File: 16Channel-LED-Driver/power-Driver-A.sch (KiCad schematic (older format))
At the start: 17 parts, among them Q1 BC413, U3 PCA9634

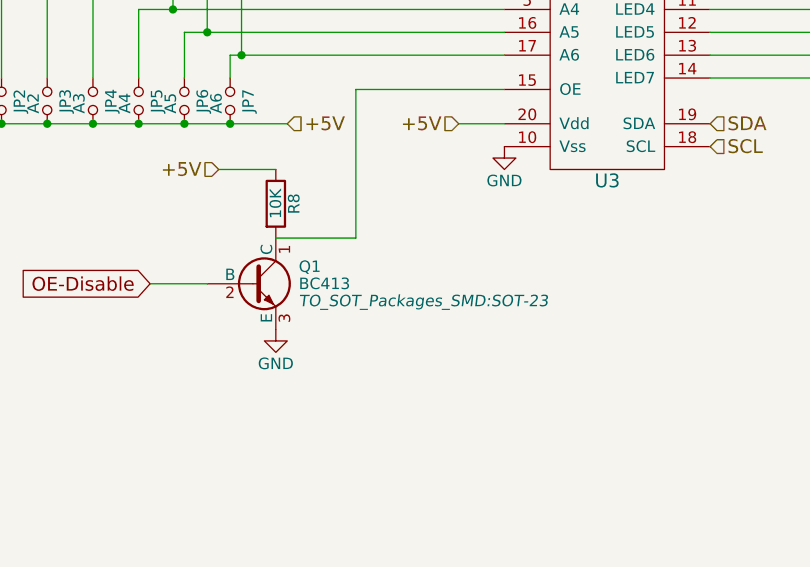
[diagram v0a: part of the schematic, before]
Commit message: Did Revision B of the 16 Channel board, also exported some gerbers
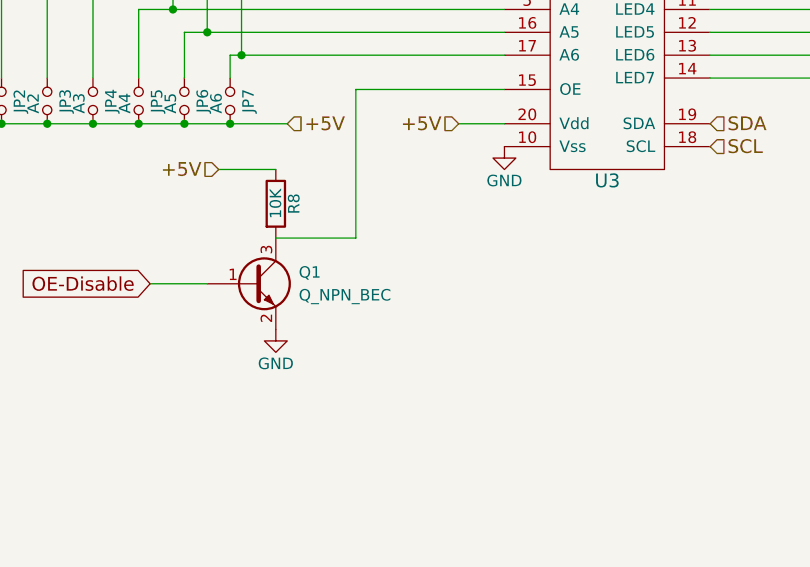
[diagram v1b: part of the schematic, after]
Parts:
- removed Q1: BC413, TO_SOT_Packages_SMD:SOT-23, symbol BC413
- added Q1: Q_NPN_BEC, TO_SOT_Packages_SMD:SOT-23, symbol Q_NPN_BEC
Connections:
- net GND: now also Q1.2 (E)
- net OE-Disable: now also Q1.1 (B)
- net at R8.2, U3.15 (OE): now also Q1.3 (C)
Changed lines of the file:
@@
 Connection ~ 2250 1150
 $Comp
-L GND #PWR011
+L GND #PWR013
 U 1 1 588BCEE3
 P 2500 1150
-F 0 "#PWR011" H 2500 900 50  0001 C CNN
+F 0 "#PWR013" H 2500 900 50  0001 C CNN
 F 1 "GND" H 2500 1000 50  0000 C CNN
 F 2 "" H 2500 1150 50  0000 C CNN
@@
 	1    0    0    -1
 $EndComp
-$Comp
-L BC413 Q1
-U 1 1 588BD03F
-P 2300 3200
-F 0 "Q1" H 2500 3275 50  0000 L CNN
-F 1 "BC413" H 2500 3200 50  0000 L CNN
-F 2 "TO_SOT_Packages_SMD:SOT-23" H 2500 3125 50  0000 L CIN
-F 3 "" H 2300 3200 50  0000 L CNN
-	1    2300 3200
-	1    0    0    -1
-$EndComp
 Wire Wire Line
 	2400 2700 2150 2700
 $Comp
-L GND #PWR012
+L GND #PWR014
 U 1 1 588BD1E2
 P 2400 3400
-F 0 "#PWR012" H 2400 3150 50  0001 C CNN
+F 0 "#PWR014" H 2400 3150 50  0001 C CNN
 F 1 "GND" H 2400 3250 50  0000 C CNN
 F 2 "" H 2400 3400 50  0000 C CNN
@@
 +5V
 $Comp
-L GND #PWR013
+L GND #PWR015
 U 1 1 588C0747
 P 3400 2600
-F 0 "#PWR013" H 3400 2350 50  0001 C CNN
+F 0 "#PWR015" H 3400 2350 50  0001 C CNN
 F 1 "GND" H 3400 2450 50  0000 C CNN
 F 2 "" H 3400 2600 50  0000 C CNN
@@
 Text HLabel 6050 4150 0    60   Input ~ 0
 +5V
+$Comp
+L Q_NPN_BEC Q1
+U 1 1 5976E7EF
+P 2300 3200
+F 0 "Q1" H 2500 3250 50  0000 L CNN
+F 1 "Q_NPN_BEC" H 2500 3150 50  0000 L CNN
+F 2 "TO_SOT_Packages_SMD:SOT-23" H 2500 3300 50  0001 C CNN
+F 3 "" H 2300 3200 50  0000 C CNN
+	1    2300 3200
+	1    0    0    -1
+$EndComp
 $EndSCHEMATC
